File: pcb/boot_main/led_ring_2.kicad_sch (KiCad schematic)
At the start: 10 parts, among them Q2 NPN

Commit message: Assign footprints
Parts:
- D5, D6, D7, D8: footprint (none) -> LED_SMD:LED_1206_3216Metric
- Q2: footprint (none) -> Package_TO_SOT_SMD:SOT-323_SC-70
- R20, R21, R22, R23, R24: footprint (none) -> Resistor_SMD:R_0603_1608Metric
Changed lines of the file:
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@@
 			)
 		)
-		(property "Footprint" ""
+		(property "Footprint" "LED_SMD:LED_1206_3216Metric"
 			(at 167.64 101.6 0)
 			(effects
@@
 			)
 		)
-		(property "Footprint" ""
+		(property "Footprint" "Package_TO_SOT_SMD:SOT-323_SC-70"
 			(at 208.28 115.57 0)
 			(effects
@@
 			)
 		)
-		(property "Footprint" ""
+		(property "Footprint" "LED_SMD:LED_1206_3216Metric"
 			(at 147.32 101.6 0)
 			(effects
@@
 			)
 		)
-		(property "Footprint" ""
+		(property "Footprint" "Resistor_SMD:R_0603_1608Metric"
 			(at 133.35 117.348 90)
 			(effects
@@
 			)
 		)
-		(property "Footprint" ""
+		(property "Footprint" "Resistor_SMD:R_0603_1608Metric"
 			(at 155.702 91.44 90)
 			(effects
@@
 			)
 		)
-		(property "Footprint" ""
+		(property "Footprint" "Resistor_SMD:R_0603_1608Metric"
 			(at 165.862 91.44 90)
 			(effects
@@
 			)
 		)
-		(property "Footprint" ""
+		(property "Footprint" "LED_SMD:LED_1206_3216Metric"
 			(at 177.8 101.6 0)
 			(effects
@@
 			)
 		)
-		(property "Footprint" ""
+		(property "Footprint" "LED_SMD:LED_1206_3216Metric"
 			(at 157.48 101.6 0)
 			(effects
@@
 			)
 		)
-		(property "Footprint" ""
+		(property "Footprint" "Resistor_SMD:R_0603_1608Metric"
 			(at 145.542 91.44 90)
 			(effects
@@
 			)
 		)
-		(property "Footprint" ""
+		(property "Footprint" "Resistor_SMD:R_0603_1608Metric"
 			(at 176.022 91.44 90)
 			(effects

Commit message: MOre layout
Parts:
- added D17, D18, D19, D20: LED, LED_SMD:LED_1206_3216Metric, symbol Device:LED
- added U7: ~, cap_pads:square_20x20mm_guide, symbol cap_pads:capacitive_pad_guide
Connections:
- new net: D17.1 (K), D18.1 (K), D19.1 (K), D20.1 (K), Q2.1 (C)
- new net: D18.2 (A), D6.1 (K)
- new net: D19.2 (A), D7.1 (K)
- new net: D17.2 (A), D5.1 (K)
- new net: D20.2 (A), D8.1 (K)
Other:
- moved on the sheet: Q2, R20

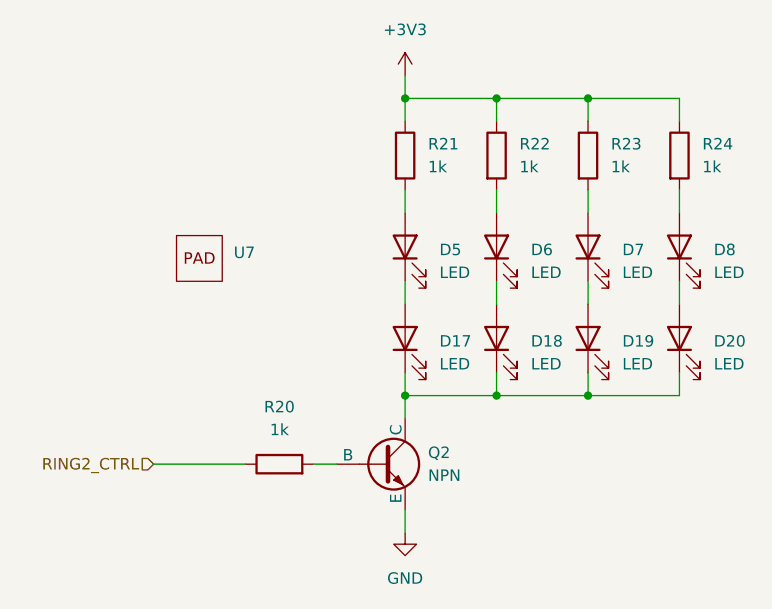
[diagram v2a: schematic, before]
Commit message: Change voltage rail on LEDs
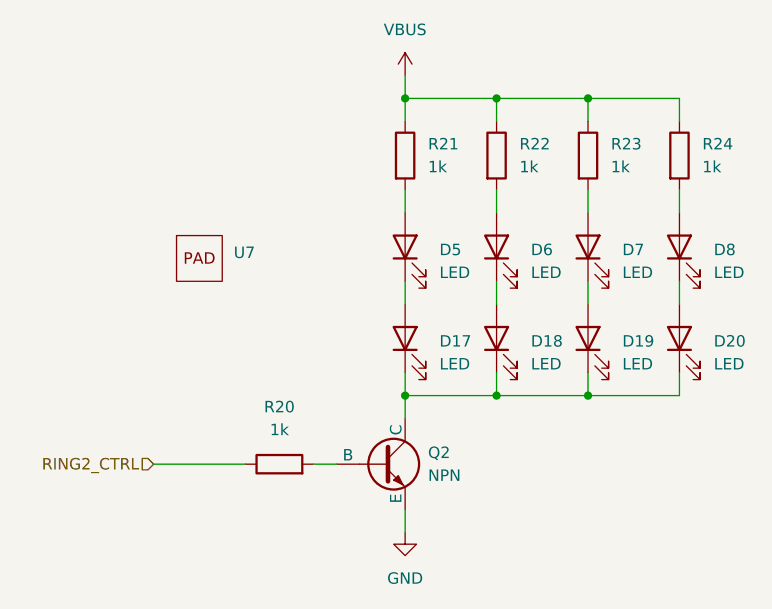
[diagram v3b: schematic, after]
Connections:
- net +3V3 renamed VBUS
